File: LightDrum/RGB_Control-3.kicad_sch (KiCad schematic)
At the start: 25 parts, among them U30 PCA9634_TSSOP20, U31 SQ2310ES_SOT23, U32 SQ2310ES_SOT23, U33 SQ2310ES_SOT23, U34 SQ2310ES_SOT23, U35 SQ2310ES_SOT23, U36 SQ2310ES_SOT23, U37 SQ2310ES_SOT23, U38 SQ2310ES_SOT23

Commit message: Add docs and gerbers for REV7
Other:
- title: RGB STRIP CONTROLLER 3 -> LightDrum
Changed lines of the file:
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@@
   (paper "A4")
   (title_block
-    (title "RGB STRIP CONTROLLER 3")
-    (rev "REV6")
+    (title "LightDrum")
+    (rev "REV7")
     (company "Daxxn Industries")
   )

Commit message: First pass over schematic (WIP)
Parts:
- R74, R76, R78, R80, R82, R84, R86, R88: value ${GATE-RES} -> 100
- R75, R77, R79, R81, R83, R85, R87, R89: value ${P-RES} -> 10K
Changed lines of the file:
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@@
   (title_block
     (title "LightDrum")
-    (rev "REV7")
+    (rev "REV8")
     (company "Daxxn Industries")
   )
@@
       (effects (font (size 1.27 1.27)) (justify right))
     )
-    (property "Value" "${GATE-RES}" (id 1) (at 133.35 74.676 0)
+    (property "Value" "100" (id 1) (at 133.35 74.676 0)
       (effects (font (size 1.27 1.27)) (justify right))
     )
@@
       (effects (font (size 1.27 1.27)) hide)
     )
-    (property "Datasheet" "C:\\Users\\Daxxn\\Documents\\Electrical\\Datasheets\\PCA9634.pdf" (id 3) (at 45.72 17.78 0)
+    (property "Datasheet" "%LOCAL_DATASHEETS%\\PCA9634.pdf" (id 3) (at 45.72 17.78 0)
       (effects (font (size 1.27 1.27)) hide)
     )
@@
       (effects (font (size 1.27 1.27)) (justify right))
     )
-    (property "Value" "${GATE-RES}" (id 1) (at 171.45 50.546 0)
+    (property "Value" "100" (id 1) (at 171.45 50.546 0)
       (effects (font (size 1.27 1.27)) (justify right))
     )
@@
       (effects (font (size 1.27 1.27)) (justify right))
     )
-    (property "Value" "${P-RES}" (id 1) (at 133.35 82.296 0)
+    (property "Value" "10K" (id 1) (at 133.35 82.296 0)
       (effects (font (size 1.27 1.27)) (justify right))
     )
@@
       (effects (font (size 1.27 1.27)) (justify right))
     )
-    (property "Value" "${P-RES}" (id 1) (at 95.25 58.166 0)
+    (property "Value" "10K" (id 1) (at 95.25 58.166 0)
       (effects (font (size 1.27 1.27)) (justify right))
     )
@@
       (effects (font (size 1.27 1.27)) (justify right))
     )
-    (property "Value" "${P-RES}" (id 1) (at 184.15 82.296 0)
+    (property "Value" "10K" (id 1) (at 184.15 82.296 0)
       (effects (font (size 1.27 1.27)) (justify right))
     )
@@
       (effects (font (size 1.27 1.27)) (justify right))
     )
-    (property "Value" "${P-RES}" (id 1) (at 120.65 58.166 0)
+    (property "Value" "10K" (id 1) (at 120.65 58.166 0)
       (effects (font (size 1.27 1.27)) (justify right))
     )
@@
       (effects (font (size 1.27 1.27)) (justify right))
     )
-    (property "Value" "${GATE-RES}" (id 1) (at 184.15 74.676 0)
+    (property "Value" "100" (id 1) (at 184.15 74.676 0)
       (effects (font (size 1.27 1.27)) (justify right))
     )
@@
       (effects (font (size 1.27 1.27)) (justify right))
     )
-    (property "Value" "${GATE-RES}" (id 1) (at 158.75 74.676 0)
+    (property "Value" "100" (id 1) (at 158.75 74.676 0)
       (effects (font (size 1.27 1.27)) (justify right))
     )
@@
       (effects (font (size 1.27 1.27)) hide)
     )
-    (property "Datasheet" "C:\\Users\\Daxxn\\Documents\\Electrical\\Datasheets\\SQ2310ES.pdf" (id 3) (at 177.8 40.64 0)
+    (property "Datasheet" "%LOCAL_DATASHEETS%\\SQ2310ES.pdf" (id 3) (at 177.8 40.64 0)
       (effects (font (size 1.27 1.27)) hide)
     )
@@
       (effects (font (size 1.27 1.27)) hide)
     )
-    (property "Datasheet" "C:\\Users\\Daxxn\\Documents\\Electrical\\Datasheets\\SQ2310ES.pdf" (id 3) (at 114.3 64.77 0)
+    (property "Datasheet" "%LOCAL_DATASHEETS%\\SQ2310ES.pdf" (id 3) (at 114.3 64.77 0)
       (effects (font (size 1.27 1.27)) hide)
     )
@@
       (effects (font (size 1.27 1.27)) hide)
     )
-    (property "Datasheet" "C:\\Users\\Daxxn\\Documents\\Electrical\\Datasheets\\SQ2310ES.pdf" (id 3) (at 101.6 40.64 0)
+    (property "Datasheet" "%LOCAL_DATASHEETS%\\SQ2310ES.pdf" (id 3) (at 101.6 40.64 0)
       (effects (font (size 1.27 1.27)) hide)
     )
@@
       (effects (font (size 1.27 1.27)) (justify right))
     )
-    (property "Value" "${P-RES}" (id 1) (at 171.45 58.166 0)
+    (property "Value" "10K" (id 1) (at 171.45 58.166 0)
       (effects (font (size 1.27 1.27)) (justify right))
     )
@@
       (effects (font (size 1.27 1.27)) (justify right))
     )
-    (property "Value" "${P-RES}" (id 1) (at 158.75 82.296 0)
+    (property "Value" "10K" (id 1) (at 158.75 82.296 0)
       (effects (font (size 1.27 1.27)) (justify right))
     )
@@
       (effects (font (size 1.27 1.27)) (justify right))
     )
-    (property "Value" "${GATE-RES}" (id 1) (at 120.65 50.546 0)
+    (property "Value" "100" (id 1) (at 120.65 50.546 0)
       (effects (font (size 1.27 1.27)) (justify right))
     )
@@
       (effects (font (size 1.27 1.27)) hide)
     )
-    (property "Datasheet" "C:\\Users\\Daxxn\\Documents\\Electrical\\Datasheets\\SQ2310ES.pdf" (id 3) (at 165.1 64.77 0)
+    (property "Datasheet" "%LOCAL_DATASHEETS%\\SQ2310ES.pdf" (id 3) (at 165.1 64.77 0)
       (effects (font (size 1.27 1.27)) hide)
     )
@@
       (effects (font (size 1.27 1.27)) (justify right))
     )
-    (property "Value" "${P-RES}" (id 1) (at 107.95 82.296 0)
+    (property "Value" "10K" (id 1) (at 107.95 82.296 0)
       (effects (font (size 1.27 1.27)) (justify right))
     )
@@
       (effects (font (size 1.27 1.27)) (justify right))
     )
-    (property "Value" "${GATE-RES}" (id 1) (at 107.95 74.676 0)
+    (property "Value" "100" (id 1) (at 107.95 74.676 0)
       (effects (font (size 1.27 1.27)) (justify right))
     )
@@
       (effects (font (size 1.27 1.27)) hide)
     )
-    (property "Datasheet" "C:\\Users\\Daxxn\\Documents\\Electrical\\Datasheets\\SQ2310ES.pdf" (id 3) (at 139.7 64.77 0)
+    (property "Datasheet" "%LOCAL_DATASHEETS%\\SQ2310ES.pdf" (id 3) (at 139.7 64.77 0)
       (effects (font (size 1.27 1.27)) hide)
     )
@@
       (effects (font (size 1.27 1.27)) (justify right))
     )
-    (property "Value" "${P-RES}" (id 1) (at 146.05 58.166 0)
+    (property "Value" "10K" (id 1) (at 146.05 58.166 0)
       (effects (font (size 1.27 1.27)) (justify right))
     )
@@
       (effects (font (size 1.27 1.27)) (justify right))
     )
-    (property "Value" "${GATE-RES}" (id 1) (at 146.05 50.546 0)
+    (property "Value" "100" (id 1) (at 146.05 50.546 0)
       (effects (font (size 1.27 1.27)) (justify right))
     )
@@
       (effects (font (size 1.27 1.27)) (justify right))
     )
-    (property "Value" "${GATE-RES}" (id 1) (at 95.25 50.546 0)
+    (property "Value" "100" (id 1) (at 95.25 50.546 0)
       (effects (font (size 1.27 1.27)) (justify right))
     )
@@
       (effects (font (size 1.27 1.27)) hide)
     )
-    (property "Datasheet" "C:\\Users\\Daxxn\\Documents\\Electrical\\Datasheets\\SQ2310ES.pdf" (id 3) (at 127 40.64 0)
+    (property "Datasheet" "%LOCAL_DATASHEETS%\\SQ2310ES.pdf" (id 3) (at 127 40.64 0)
       (effects (font (size 1.27 1.27)) hide)
     )
@@
       (effects (font (size 1.27 1.27)) hide)
     )
-    (property "Datasheet" "C:\\Users\\Daxxn\\Documents\\Electrical\\Datasheets\\SQ2310ES.pdf" (id 3) (at 152.4 40.64 0)
+    (property "Datasheet" "%LOCAL_DATASHEETS%\\SQ2310ES.pdf" (id 3) (at 152.4 40.64 0)
       (effects (font (size 1.27 1.27)) hide)
     )
@@
       (effects (font (size 1.27 1.27)) hide)
     )
-    (property "Datasheet" "C:\\Users\\Daxxn\\Documents\\Electrical\\Datasheets\\SQ2310ES.pdf" (id 3) (at 190.5 64.77 0)
-      (effects (font (size 1.27 1.27)) hide)
-    )
+    (property "Datasheet" "%LOCAL_DATASHEETS%\\SQ2310ES.pdf" (id 3) (at 190.5 64.77 0)
+      (effects (font (size 1.27 1.27)) hide)
+    )

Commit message: General component placement
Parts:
- U501: renamed from U30; PartNumber (none) -> 0806-0003
- U502: renamed from U31; PartNumber (none) -> 0703-0001
- U503: renamed from U33; PartNumber (none) -> 0703-0001
- U504: renamed from U35; PartNumber (none) -> 0703-0001
- U505: renamed from U37; PartNumber (none) -> 0703-0001
- U506: renamed from U32; PartNumber (none) -> 0703-0001
- U507: renamed from U34; PartNumber (none) -> 0703-0001
- U508: renamed from U36; PartNumber (none) -> 0703-0001
- U509: renamed from U38; PartNumber (none) -> 0703-0001
- renumbered R74 to R501, R78 to R502, R82 to R503, R86 to R504, R75 to R505, R79 to R506, R83 to R507, R87 to R508, R76 to R509, R80 to R510, R84 to R511, R88 to R512, R77 to R513, R81 to R514, R85 to R515, R89 to R516

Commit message: Simplify analog power supply and add some routing
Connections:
- net GND: now also U501.2 (A1), U501.5 (A4); no longer U501.16 (A5), U501.4 (A3)
- net LED3-B-SIG: now also U501.14 (LED7); no longer U501.6 (LED0)
- net LED4-B-SIG: now also U501.8 (LED2); no longer U501.11 (LED4)
- net LED4-G-SIG: now also U501.12 (LED5); no longer U501.8 (LED2)
- net LED4-R-SIG: now also U501.6 (LED0); no longer U501.13 (LED6)
- net LED7-B-SIG: now also U501.13 (LED6); no longer U501.7 (LED1)
- net LED8-B-SIG: now also U501.9 (LED3); no longer U501.14 (LED7)
- net LED8-G-SIG: now also U501.11 (LED4); no longer U501.12 (LED5)
- net LED8-R-SIG: now also U501.7 (LED1); no longer U501.9 (LED3)
- net VCC renamed VDD
- net VDD: now also U501.16 (A5), U501.4 (A3); no longer U501.2 (A1), U501.5 (A4)
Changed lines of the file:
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@@
     (company "Daxxn Industries")
   )
-  (junction (at 35.56 54.61) (diameter 0) (color 0 0 0 0)
-  )
   (junction (at 114.3 64.77) (diameter 0) (color 0 0 0 0)
   )
   (junction (at 160.02 77.47) (diameter 0) (color 0 0 0 0)
   )
-  (junction (at 34.29 44.45) (diameter 0) (color 0 0 0 0)
-  )
   (junction (at 165.1 85.09) (diameter 0) (color 0 0 0 0)
   )
@@
   (junction (at 172.72 53.34) (diameter 0) (color 0 0 0 0)
   )
+  (junction (at 34.29 49.53) (diameter 0) (color 0 0 0 0)
+  )
+  (junction (at 35.56 52.07) (diameter 0) (color 0 0 0 0)
+  )
   (junction (at 185.42 77.47) (diameter 0) (color 0 0 0 0)
   )
@@
   (junction (at 139.7 85.09) (diameter 0) (color 0 0 0 0)
   )
-  (junction (at 35.56 49.53) (diameter 0) (color 0 0 0 0)
+  (junction (at 35.56 44.45) (diameter 0) (color 0 0 0 0)
   )
   (junction (at 172.72 60.96) (diameter 0) (color 0 0 0 0)
@@
   )
   (bus_entry (at 157.48 67.31) (size 2.54 2.54)
-    (stroke (width 0) (type default) (color 0 0 0 0))
-  )
-  (wire (pts (xy 34.29 52.07) (xy 36.83 52.07))
     (stroke (width 0) (type default) (color 0 0 0 0))
   )
@@
     (stroke (width 0) (type default) (color 0 0 0 0))
   )
-  (wire (pts (xy 36.83 49.53) (xy 35.56 49.53))
-    (stroke (width 0) (type default) (color 0 0 0 0))
-  )
   (wire (pts (xy 34.29 44.45) (xy 34.29 46.99))
     (stroke (width 0) (type default) (color 0 0 0 0))
@@
     (stroke (width 0) (type default) (color 0 0 0 0))
   )
-  (wire (pts (xy 35.56 49.53) (xy 35.56 54.61))
-    (stroke (width 0) (type default) (color 0 0 0 0))
-  )
   (wire (pts (xy 160.02 76.2) (xy 160.02 77.47))
     (stroke (width 0) (type default) (color 0 0 0 0))
@@
     (stroke (width 0) (type default) (color 0 0 0 0))
   )
+  (wire (pts (xy 35.56 44.45) (xy 35.56 52.07))
+    (stroke (width 0) (type default) (color 0 0 0 0))
+  )
   (wire (pts (xy 190.5 81.28) (xy 190.5 85.09))
     (stroke (width 0) (type default) (color 0 0 0 0))
@@
     (stroke (width 0) (type default) (color 0 0 0 0))
   )
-  (wire (pts (xy 35.56 41.91) (xy 35.56 49.53))
+  (wire (pts (xy 35.56 41.91) (xy 35.56 44.45))
     (stroke (width 0) (type default) (color 0 0 0 0))
   )
@@
     (stroke (width 0) (type default) (color 0 0 0 0))
   )
+  (wire (pts (xy 35.56 44.45) (xy 36.83 44.45))
+    (stroke (width 0) (type default) (color 0 0 0 0))
+  )
+  (wire (pts (xy 35.56 52.07) (xy 36.83 52.07))
+    (stroke (width 0) (type default) (color 0 0 0 0))
+  )
   (wire (pts (xy 45.72 26.67) (xy 45.72 27.94))
     (stroke (width 0) (type default) (color 0 0 0 0))
@@
     (stroke (width 0) (type default) (color 0 0 0 0))
   )
-  (wire (pts (xy 35.56 54.61) (xy 35.56 57.15))
+  (wire (pts (xy 35.56 52.07) (xy 35.56 57.15))
     (stroke (width 0) (type default) (color 0 0 0 0))
   )
@@
     (stroke (width 0) (type default) (color 0 0 0 0))
   )
+  (wire (pts (xy 34.29 54.61) (xy 36.83 54.61))
+    (stroke (width 0) (type default) (color 0 0 0 0))
+  )
   (wire (pts (xy 35.56 57.15) (xy 36.83 57.15))
     (stroke (width 0) (type default) (color 0 0 0 0))
@@
     (stroke (width 0) (type default) (color 0 0 0 0))
   )
+  (wire (pts (xy 34.29 49.53) (xy 36.83 49.53))
+    (stroke (width 0) (type default) (color 0 0 0 0))
+  )
+  (wire (pts (xy 34.29 49.53) (xy 34.29 54.61))
+    (stroke (width 0) (type default) (color 0 0 0 0))
+  )
   (bus (pts (xy 182.88 64.77) (xy 182.88 67.31))
     (stroke (width 0) (type default) (color 0 0 0 0))
@@
     (stroke (width 0) (type default) (color 0 0 0 0))
   )
-  (wire (pts (xy 34.29 44.45) (xy 36.83 44.45))
-    (stroke (width 0) (type default) (color 0 0 0 0))
-  )
   (wire (pts (xy 96.52 53.34) (xy 97.79 53.34))
     (stroke (width 0) (type default) (color 0 0 0 0))
@@
     (stroke (width 0) (type default) (color 0 0 0 0))
   )
-  (wire (pts (xy 34.29 46.99) (xy 34.29 52.07))
+  (wire (pts (xy 34.29 46.99) (xy 34.29 49.53))
     (stroke (width 0) (type default) (color 0 0 0 0))
   )
@@
   )
   (bus (pts (xy 88.9 64.77) (xy 106.68 64.77))
-    (stroke (width 0) (type default) (color 0 0 0 0))
-  )
-  (wire (pts (xy 35.56 54.61) (xy 36.83 54.61))
     (stroke (width 0) (type default) (color 0 0 0 0))
   )
@@
     (effects (font (size 1.27 1.27)) (justify left bottom))
   )
-  (label "LED4-R-SIG" (at 55.88 50.8 0)
+  (label "LED4-R-SIG" (at 55.88 35.56 0)
     (effects (font (size 1.27 1.27)) (justify left bottom))
   )
@@
     (effects (font (size 1.27 1.27)) (justify left bottom))
   )
-  (label "LED8-G-SIG" (at 55.88 48.26 0)
+  (label "LED8-G-SIG" (at 55.88 45.72 0)
     (effects (font (size 1.27 1.27)) (justify left bottom))
   )
@@
     (effects (font (size 1.27 1.27)) (justify left bottom))
   )
-  (label "LED8-R-SIG" (at 55.88 43.18 0)
-    (effects (font (size 1.27 1.27)) (justify left bottom))
-  )
-  (label "LED4-B-SIG" (at 55.88 45.72 0)
-    (effects (font (size 1.27 1.27)) (justify left bottom))
-  )
-  (label "LED7-B-SIG" (at 55.88 38.1 0)
+  (label "LED8-R-SIG" (at 55.88 38.1 0)
+    (effects (font (size 1.27 1.27)) (justify left bottom))
+  )
+  (label "LED4-B-SIG" (at 55.88 40.64 0)
+    (effects (font (size 1.27 1.27)) (justify left bottom))
+  )
+  (label "LED7-B-SIG" (at 55.88 50.8 0)
     (effects (font (size 1.27 1.27)) (justify left bottom))
   )
@@
     (effects (font (size 1.27 1.27)) (justify left bottom))
   )
-  (label "LED4-G-SIG" (at 55.88 40.64 0)
-    (effects (font (size 1.27 1.27)) (justify left bottom))
-  )
-  (label "LED8-B-SIG" (at 55.88 53.34 0)
+  (label "LED4-G-SIG" (at 55.88 48.26 0)
+    (effects (font (size 1.27 1.27)) (justify left bottom))
+  )
+  (label "LED8-B-SIG" (at 55.88 43.18 0)
     (effects (font (size 1.27 1.27)) (justify left bottom))
   )
@@
     (effects (font (size 1.27 1.27)) (justify left bottom))
   )
-  (label "LED3-B-SIG" (at 55.88 35.56 0)
+  (label "LED3-B-SIG" (at 55.88 53.34 0)
     (effects (font (size 1.27 1.27)) (justify left bottom))
   )
@@
     (pin "9")
   )
+  (symbol (lib_id "power:VDD") (at 20.32 43.18 0) (unit 1)
+    (in_bom yes) (on_board yes)
+    (property "Reference" "#PWR0130" (id 0) (at 20.32 46.99 0)
+      (effects (font (size 1.27 1.27)) hide)
+    )
+    (property "Value" "VDD" (id 1) (at 20.32 39.37 0))
+    (property "Footprint" "" (id 2) (at 20.32 43.18 0)
+      (effects (font (size 1.27 1.27)) hide)
+    )
+    (property "Datasheet" "" (id 3) (at 20.32 43.18 0)
+      (effects (font (size 1.27 1.27)) hide)
+    )
+    (pin "1")
+  )
   (symbol (lib_id "Device:R_Small_US") (at 172.72 49.53 0) (unit 1)
     (in_bom yes) (on_board yes)
@@
     (pin "1")
   )
-  (symbol (lib_id "power:VCC") (at 45.72 26.67 0) (unit 1)
-    (in_bom yes) (on_board yes)
-    (property "Reference" "#PWR0501" (id 0) (at 45.72 30.48 0)
-      (effects (font (size 1.27 1.27)) hide)
-    )
-    (property "Value" "VCC" (id 1) (at 45.72 22.86 0))
-    (property "Footprint" "" (id 2) (at 45.72 26.67 0)
-      (effects (font (size 1.27 1.27)) hide)
-    )
-    (property "Datasheet" "" (id 3) (at 45.72 26.67 0)
-      (effects (font (size 1.27 1.27)) hide)
-    )
-    (pin "1")
-  )
   (symbol (lib_id "Device:R_Small_US") (at 160.02 73.66 0) (unit 1)
     (in_bom yes) (on_board yes)
@@
     (pin "2")
   )
-  (symbol (lib_id "power:VCC") (at 20.32 43.18 0) (unit 1)
-    (in_bom yes) (on_board yes)
-    (property "Reference" "#PWR0502" (id 0) (at 20.32 46.99 0)
-      (effects (font (size 1.27 1.27)) hide)
-    )
-    (property "Value" "VCC" (id 1) (at 20.32 39.37 0))
-    (property "Footprint" "" (id 2) (at 20.32 43.18 0)
-      (effects (font (size 1.27 1.27)) hide)
-    )
-    (property "Datasheet" "" (id 3) (at 20.32 43.18 0)
-      (effects (font (size 1.27 1.27)) hide)
-    )
+  (symbol (lib_id "power:VDD") (at 45.72 26.67 0) (unit 1)
+    (in_bom yes) (on_board yes)
+    (property "Reference" "#PWR0129" (id 0) (at 45.72 30.48 0)
+      (effects (font (size 1.27 1.27)) hide)
+    )
+    (property "Value" "VDD" (id 1) (at 45.72 22.86 0))
+    (property "Footprint" "" (id 2) (at 45.72 26.67 0)
+      (effects (font (size 1.27 1.27)) hide)
+    )
+    (property "Datasheet" "" (id 3) (at 45.72 26.67 0)
+      (effects (font (size 1.27 1.27)) hide)
+    )

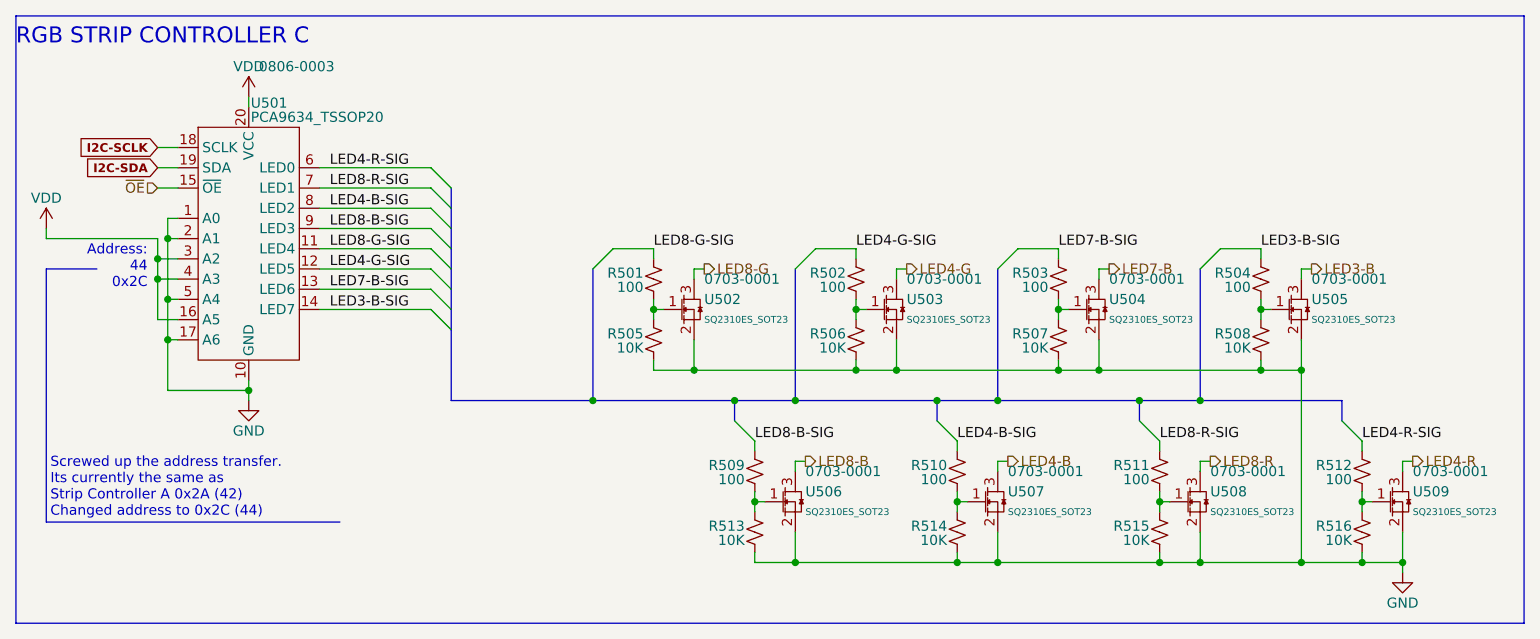
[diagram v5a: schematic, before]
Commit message: Replace old MOSFETs with a more compact package
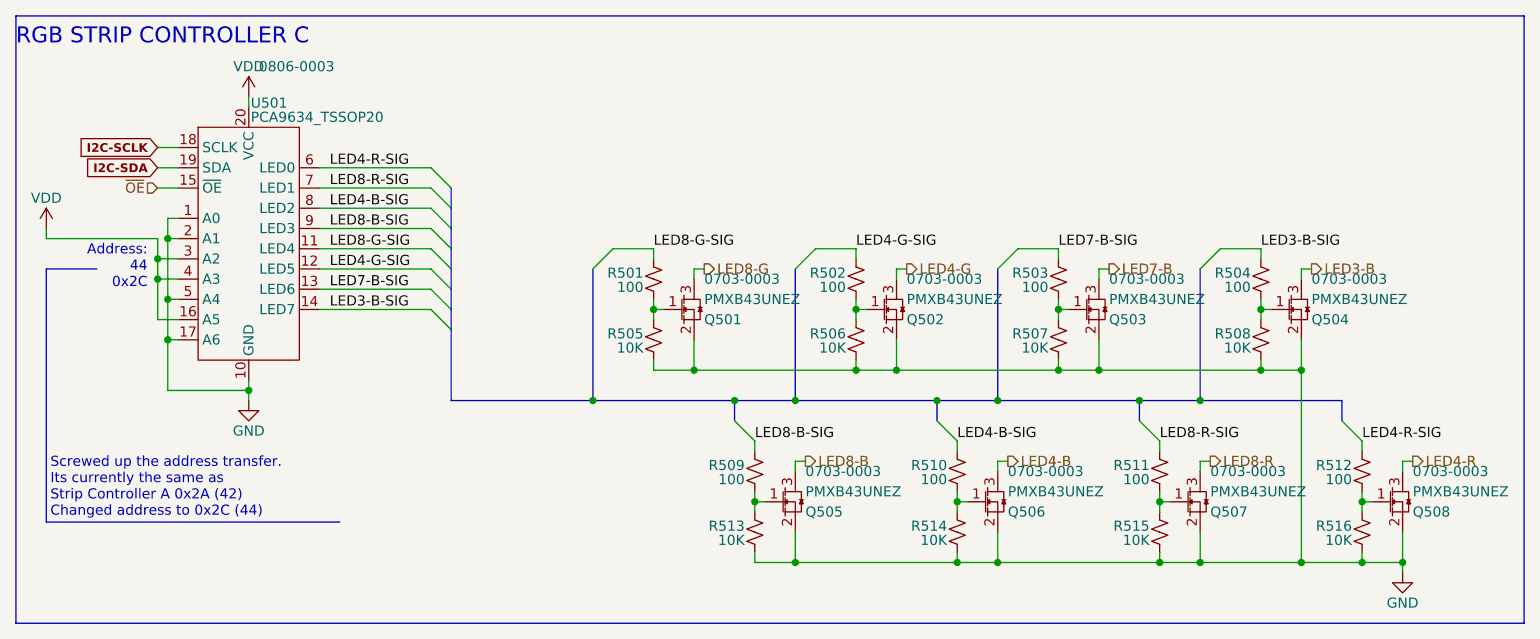
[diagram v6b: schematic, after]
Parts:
- removed U502, U503, U504, U505, U506, U507, U508, U509: SQ2310ES_SOT23, Package_TO_SOT_SMD:SOT-23, symbol Daxxn_Transistors:SQ2310ES_SOT23
- added Q501, Q502, Q503, Q504, Q505, Q506, Q507, Q508: PMXB43UNEZ, Daxxn_Packages:DFN1010D-3, symbol Daxxn_Transistors:PMXB43UNEZ
- R501, R502, R503, R504, R505, R506, R507, R508, R509, R510, R511, R512, R513, R514, R515, R516: footprint Resistor_SMD:R_0805_2012Metric -> Resistor_SMD:R_0603_1608Metric
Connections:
- net GND: now also Q501.2 (S), Q502.2 (S), Q503.2 (S), Q504.2 (S), Q505.2 (S), Q506.2 (S), Q507.2 (S), Q508.2 (S)
- net LED3-B: now also Q504.3 (D)
- net LED4-B: now also Q506.3 (D)
- net LED4-G: now also Q502.3 (D)
- net LED4-R: now also Q508.3 (D)
- net LED7-B: now also Q503.3 (D)
- net LED8-B: now also Q505.3 (D)
- net LED8-G: now also Q501.3 (D)
- net LED8-R: now also Q507.3 (D)
- net at R510.2, R514.1: now also Q506.1 (G)
- net at R504.2, R508.1: now also Q504.1 (G)
- net at R501.2, R505.1: now also Q501.1 (G)
- net at R512.2, R516.1: now also Q508.1 (G)
- net at R502.2, R506.1: now also Q502.1 (G)
- net at R511.2, R515.1: now also Q507.1 (G)
- net at R509.2, R513.1: now also Q505.1 (G)
- net at R503.2, R507.1: now also Q503.1 (G)
